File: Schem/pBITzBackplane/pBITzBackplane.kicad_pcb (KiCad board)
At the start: 4 copper layers, 243.8 x 243.8 mm, 54 parts, among them J1 ATX-24, J2 pBITzBus, J3 pBITzBus, J4 pBITzBus, J5 pBITzBus, J6 pBITzBus, J7 Conn_02x10_Odd_Even, Q1 BSS138, SW1 SW_Push, U1 ATtiny85-20P

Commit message: Fixed board
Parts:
- removed R2, R3, R4: 4k7, Resistor_SMD:R_0603_1608Metric
- added R6: 10k, Resistor_SMD:R_1206_3216Metric, F.Cu at (351.5, 396.3)
- added R7: 10k, Resistor_SMD:R_1206_3216Metric, F.Cu at (354.0, 396.3)
- added R8: 10k, Resistor_SMD:R_1206_3216Metric, F.Cu at (348.9, 396.3)
- C10, C11, C12, C13, C14, C15, C16, C17, C8, C9: footprint Capacitor_SMD:C_0603_1608Metric -> Capacitor_SMD:C_1206_3216Metric
- H1: value MountingHole (F) -> MountingHole; footprint MountingHole:MountingHole_3.2mm_M3_Pad_Via -> MountingHole:MountingHole_3.5mm_Pad_TopBottom
- H10, H11, H12, H13, H2, H3, H4, H5, H6, H7, H8, H9: footprint MountingHole:MountingHole_3.2mm_M3_Pad_Via -> MountingHole:MountingHole_3.5mm_Pad_TopBottom
- R1, R19, R20, R5: footprint Resistor_SMD:R_0603_1608Metric -> Resistor_SMD:R_1206_3216Metric
- moved C11 1.55 mm to (231.8, 228.5)
- moved C10 1.53 mm to (211.6, 228.5)
- moved C8 1.53 mm to (171.0, 228.5)
- moved C9 1.44 mm to (191.3, 228.5)
- moved C13 1.15 mm to (186.4, 228.5)
- moved C15 1.13 mm to (166.1, 228.5)
- moved C14 1.13 mm to (227.0, 228.5)
- moved C12 1.08 mm to (206.7, 228.5)
- moved C16 0.81 mm to (277.8, 223.3)
- moved C17 0.81 mm to (277.8, 225.8)
- moved R19 0.80 mm to (324.6, 387.1)
- moved R20 0.80 mm to (330.5, 387.1)
- moved R5 0.44 mm to (342.2, 393.7)
- turned R1 to 180 degrees
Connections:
- H1 pad 1: (no net) -> GND
- H10 pad 1: (no net) -> GND
- H11 pad 1: (no net) -> GND
- H12 pad 1: (no net) -> GND
- H13 pad 1: (no net) -> GND
- H2 pad 1: (no net) -> GND
- H3 pad 1: (no net) -> GND
- H4 pad 1: (no net) -> GND
- H5 pad 1: (no net) -> GND
- H6 pad 1: (no net) -> GND
- H7 pad 1: (no net) -> GND
- H8 pad 1: (no net) -> GND
- H9 pad 1: (no net) -> GND
- J2 pad A3: /Backplane/~{PWR_OFF_RQ} -> /Backplane/~{SHUTDOWN_RQ}
- J3 pad A3: /Backplane/~{PWR_OFF_RQ} -> /Backplane/~{SHUTDOWN_RQ}
- J4 pad A3: /Backplane/~{PWR_OFF_RQ} -> /Backplane/~{SHUTDOWN_RQ}
- J5 pad A3: /Backplane/~{PWR_OFF_RQ} -> /Backplane/~{SHUTDOWN_RQ}
- J6 pad A3: /Backplane/~{PWR_OFF_RQ} -> /Backplane/~{SHUTDOWN_RQ}
- U1 pad 2: Net-(U1-XTAL1/PB3) -> /Backplane/~{SHUTDOWN_RQ}
- U1 pad 3: Net-(U1-XTAL2/PB4) -> /Backplane/~{PWR_OFF}
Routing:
- net /Backplane/~{PWR_OFF_RQ}: track 340.9 -> 0.00 mm, vias 2 -> 0
- net /Backplane/~{SHUTDOWN_RQ}: track 0.00 -> 325.9 mm, vias 0 -> 1
- net /Backplane/~{PWR_OFF}: track 338.4 -> 322.8 mm, vias 2 -> 1
- net +5V_AON: track 75.8 -> 88.4 mm
- net Net-(Q1-G): track 2.19 -> 14.3 mm
- net GND: track 15.3 -> 24.0 mm, vias 281 -> 282
- net +3V3: track 536.4 -> 544.4 mm
- net Net-(U1-XTAL2/PB4): track 3.25 -> 0.00 mm
- net +5V: track 35.1 -> 37.4 mm
- net Net-(D1-K): track 2.00 -> 4.09 mm
- net Net-(U1-XTAL1/PB3): track 1.80 -> 0.00 mm
- net Net-(R1-Pad2): track 2.63 -> 4.08 mm
- net /Power/PWR_SW: track 1.81 -> 3.24 mm
- net Net-(D2-K): track 3.18 -> 4.23 mm
- net Net-(U1-~{RESET}/PB5): track 1.88 -> 2.43 mm

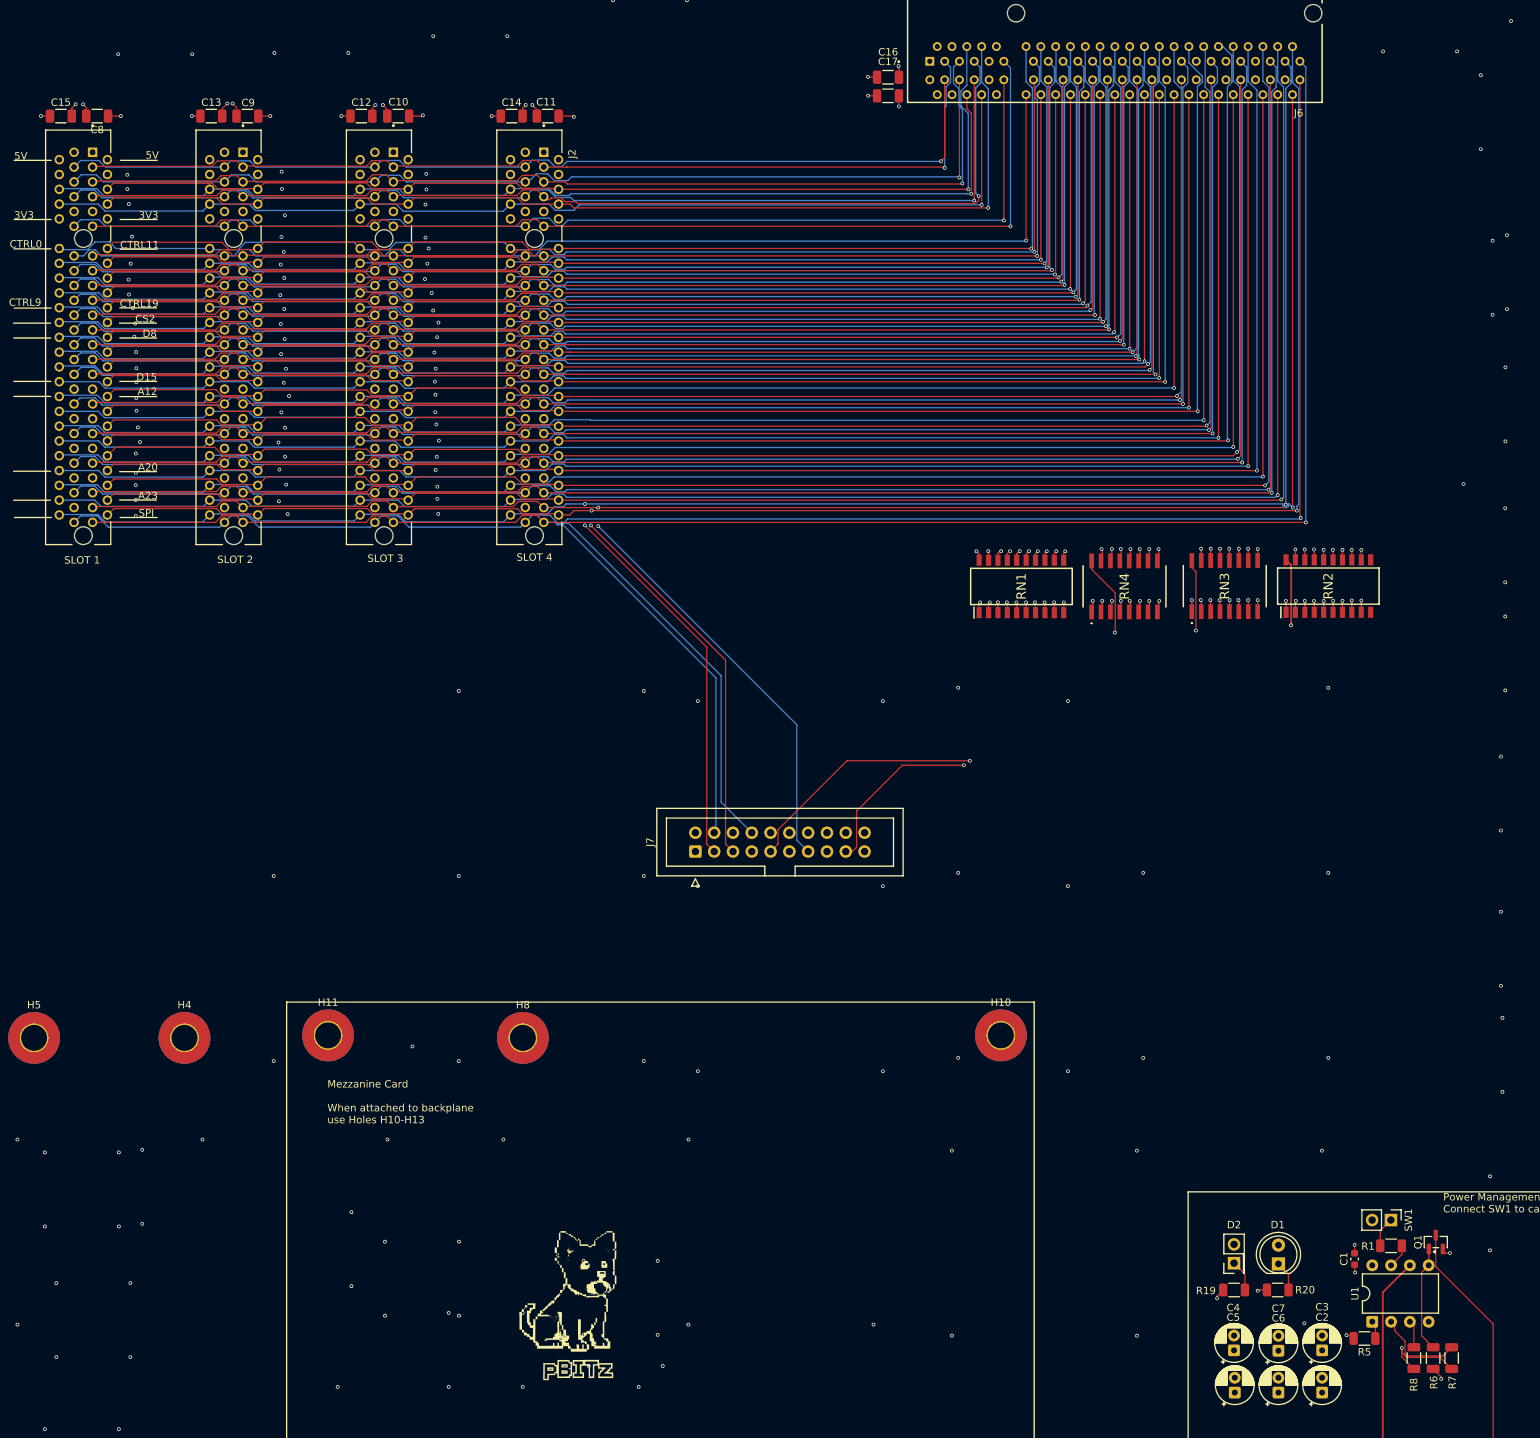
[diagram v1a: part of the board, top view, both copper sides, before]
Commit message: Made the footprint bigger to facilitate soldering.
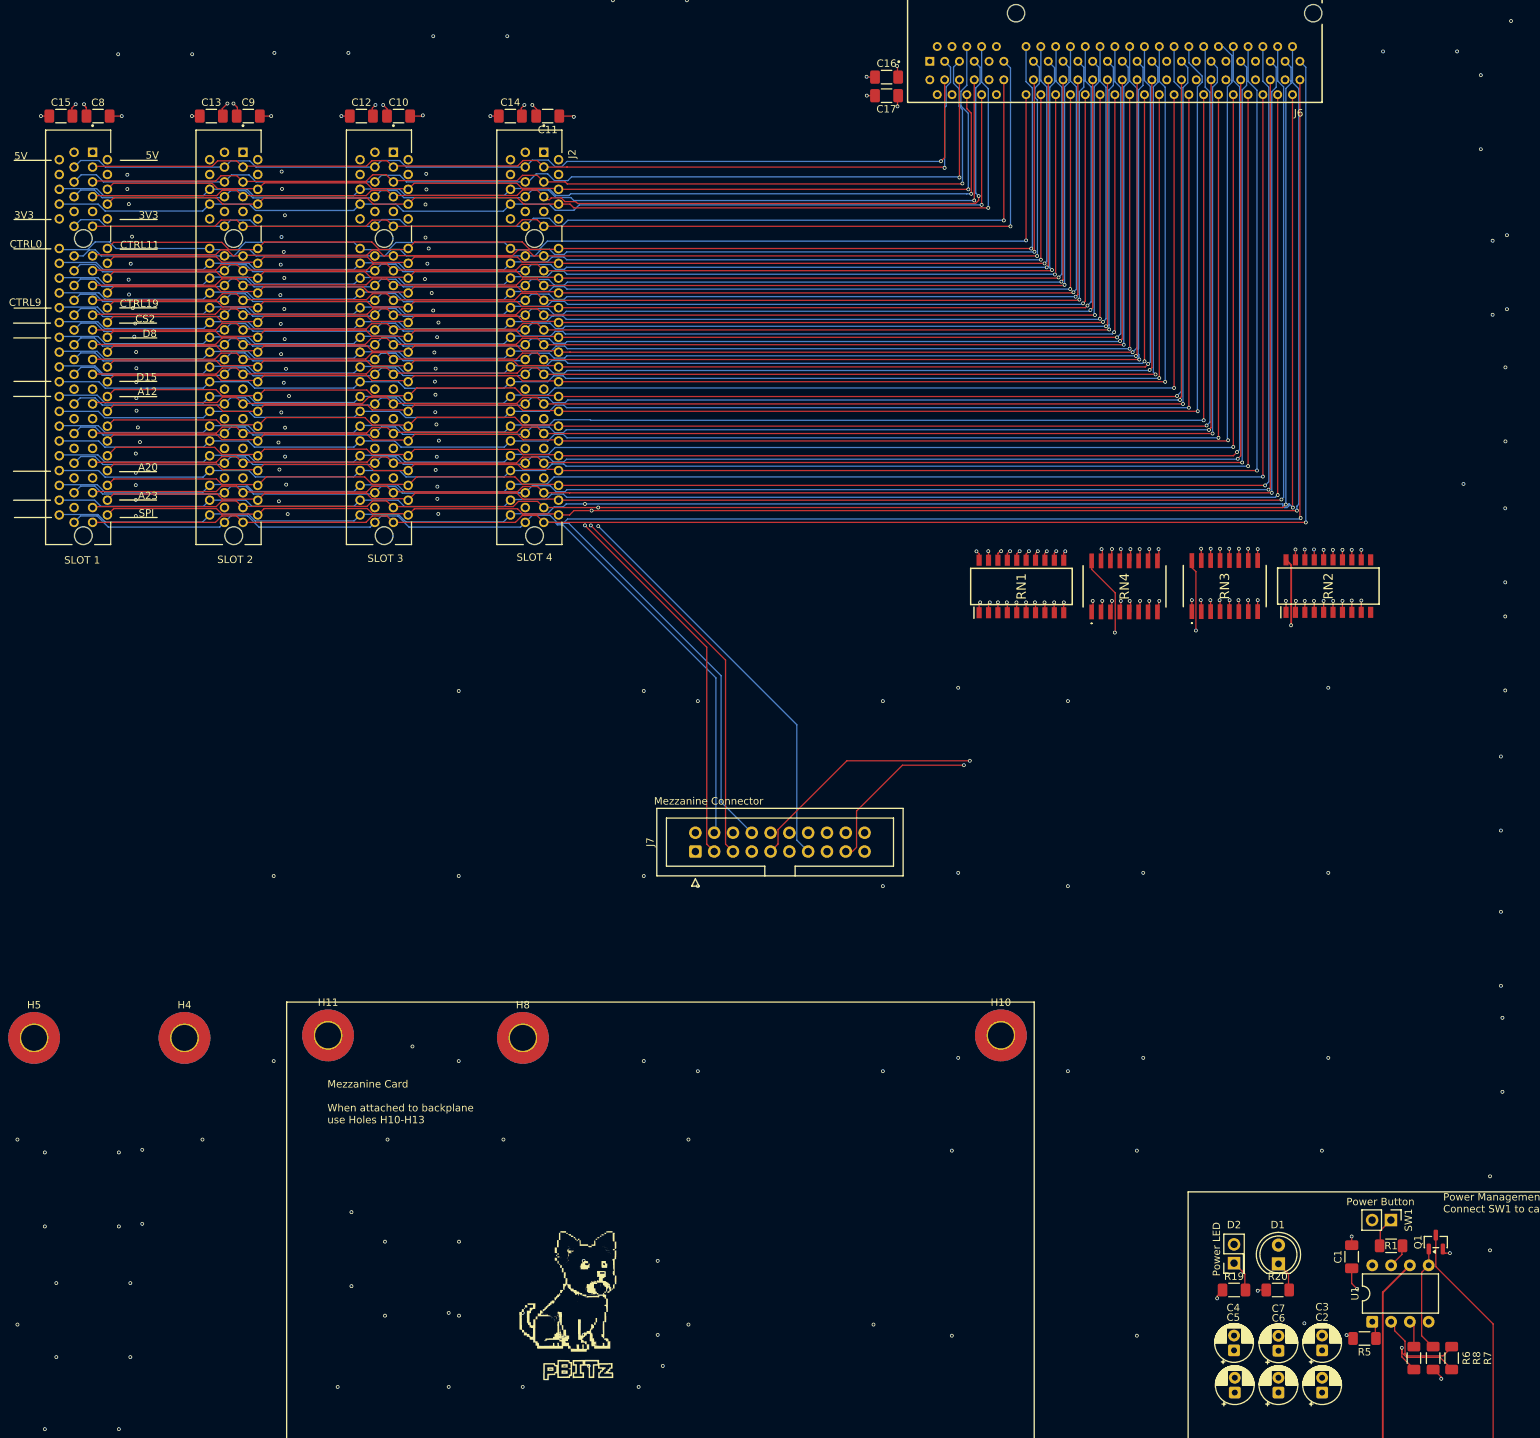
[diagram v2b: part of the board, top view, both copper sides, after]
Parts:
- C1: footprint Capacitor_SMD:C_0603_1608Metric -> Capacitor_SMD:C_1206_3216Metric_Pad1.33x1.80mm_HandSolder
- C10, C11, C12, C13, C14, C15, C16, C17, C8, C9: footprint Capacitor_SMD:C_1206_3216Metric -> Capacitor_SMD:C_1206_3216Metric_Pad1.33x1.80mm_HandSolder
- R1, R19, R20, R5, R6, R7, R8: footprint Resistor_SMD:R_1206_3216Metric -> Resistor_SMD:R_1206_3216Metric_Pad1.30x1.75mm_HandSolder
- moved C1 0.50 mm to (340.5, 382.6)
- moved C16 0.19 mm to (277.6, 223.3)
- moved C17 0.19 mm to (277.6, 225.8)
- moved C14 0.17 mm to (226.8, 228.5)
- moved C8 0.12 mm to (171.1, 228.5)
- moved C9 0.12 mm to (191.4, 228.5)
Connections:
- H1 pad 1: GND -> (no net)
- H10 pad 1: GND -> (no net)
- H11 pad 1: GND -> (no net)
- H12 pad 1: GND -> (no net)
- H13 pad 1: GND -> (no net)
- H2 pad 1: GND -> (no net)
- H3 pad 1: GND -> (no net)
- H4 pad 1: GND -> (no net)
- H5 pad 1: GND -> (no net)
- H6 pad 1: GND -> (no net)
- H7 pad 1: GND -> (no net)
- H8 pad 1: GND -> (no net)
- H9 pad 1: GND -> (no net)
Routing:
- net +5V_AON: track 88.4 -> 89.6 mm
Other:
- board text added: "Mezzanine Connector"
- board text added: "Power Button"
- board text added: "Power LED"
